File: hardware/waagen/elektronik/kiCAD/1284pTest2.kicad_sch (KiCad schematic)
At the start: 3 parts, among them J3 Conn_02x05_Odd_Even, U6 DS18B20

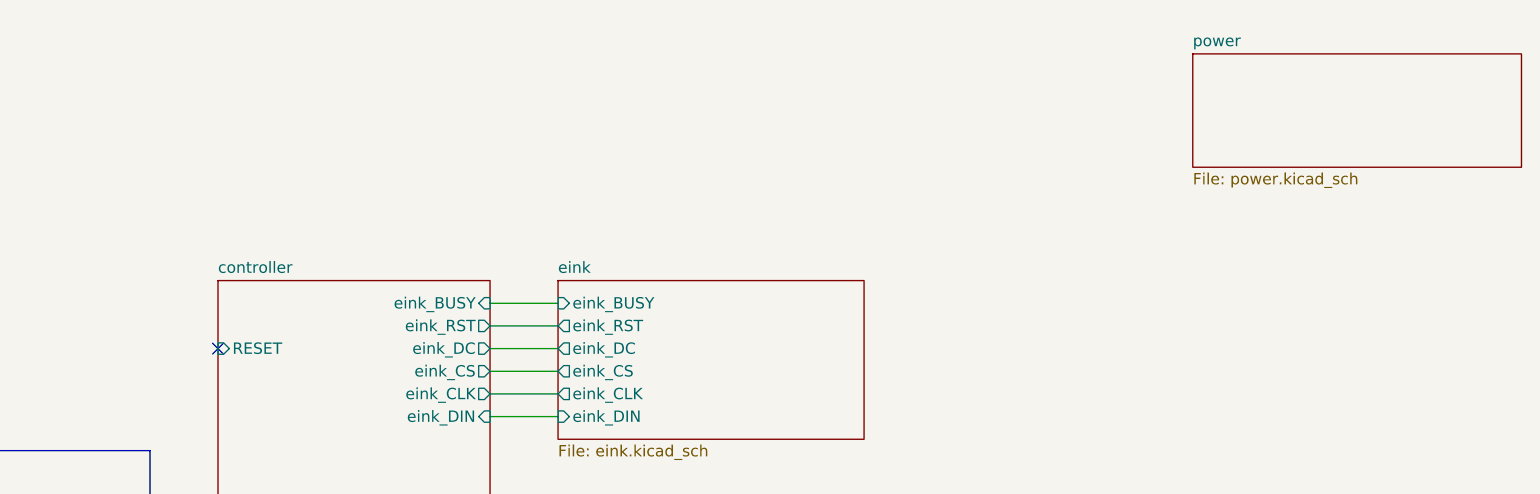
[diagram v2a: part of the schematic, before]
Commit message: second LDO for eink added
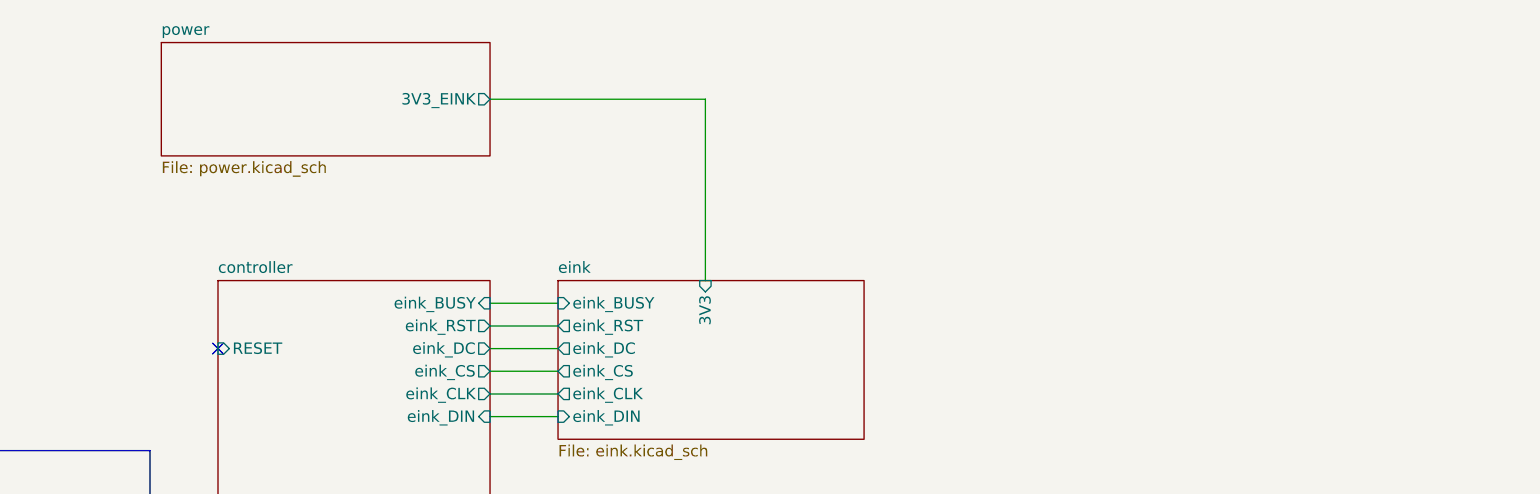
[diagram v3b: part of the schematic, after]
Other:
- sheet eink ports: added 3V3; removed none
- sheet power ports: added 3V3_EINK; removed none
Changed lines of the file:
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@@
+    (stroke (width 0) (type default) (color 0 0 0 0))
+  )
+  (wire (pts (xy 149.86 43.18) (xy 149.86 63.5))
     (stroke (width 0) (type default) (color 0 0 0 0))
   )
@@
   )
   (wire (pts (xy 62.23 93.98) (xy 62.23 95.25))
+    (stroke (width 0) (type default) (color 0 0 0 0))
+  )
+  (wire (pts (xy 125.73 43.18) (xy 149.86 43.18))
     (stroke (width 0) (type default) (color 0 0 0 0))
   )
@@
       (effects (font (size 1.27 1.27)) (justify left))
     )
+    (pin "3V3" input (at 149.86 63.5 90)
+      (effects (font (size 1.27 1.27)) (justify right))
+    )
   )
   (sheet (at 133.35 109.22) (size 34.29 21.59) (fields_autoplaced)
@@
     )
   )
-  (sheet (at 204.47 38.1) (size 36.83 12.7) (fields_autoplaced)
+  (sheet (at 88.9 36.83) (size 36.83 12.7) (fields_autoplaced)
     (stroke (width 0.1524) (type solid) (color 0 0 0 0))
     (fill (color 0 0 0 0.0000))
-    (property "Sheet name" "power" (id 0) (at 204.47 37.3884 0)
+    (property "Sheet name" "power" (id 0) (at 88.9 36.1184 0)
       (effects (font (size 1.27 1.27)) (justify left bottom))
     )
-    (property "Sheet file" "power.kicad_sch" (id 1) (at 204.47 51.3846 0)
+    (property "Sheet file" "power.kicad_sch" (id 1) (at 88.9 50.1146 0)
       (effects (font (size 1.27 1.27)) (justify left top))
+    )
+    (pin "3V3_EINK" output (at 125.73 43.18 0)
+      (effects (font (size 1.27 1.27)) (justify right))
     )
   )
@@
       (reference "#PWR040") (unit 1) (value "GND") (footprint "")
     )
-    (path "/30494837-48ad-4be2-9240-423a5e323ded/63635667-90c7-4555-8fb7-34d9681a99c7"
-      (reference "#PWR041") (unit 1) (value "VCC") (footprint "")
+    (path "/ac84ca8c-8952-41f4-b081-d474e4c76964/6be68c0c-8fc3-4b67-bece-9f51ba607cb0"
+      (reference "#PWR041") (unit 1) (value "GND") (footprint "")
+    )
+    (path "/ac84ca8c-8952-41f4-b081-d474e4c76964/663da0bb-040e-43a6-982a-c4e18537fdce"
+      (reference "#PWR042") (unit 1) (value "GND") (footprint "")
+    )
+    (path "/ac84ca8c-8952-41f4-b081-d474e4c76964/06bfdbdf-3e53-42a3-abc9-fd9ec56e91ec"
+      (reference "#PWR043") (unit 1) (value "GND") (footprint "")
+    )
+    (path "/ac84ca8c-8952-41f4-b081-d474e4c76964/d69a5db1-1044-402e-a9d0-ac8cc7d19c6c"
+      (reference "#PWR044") (unit 1) (value "GND") (footprint "")
+    )
+    (path "/ac84ca8c-8952-41f4-b081-d474e4c76964/1f362bf5-d35e-41ae-9345-c3c2ec77a158"
+      (reference "#PWR045") (unit 1) (value "GND") (footprint "")
+    )
+    (path "/ac84ca8c-8952-41f4-b081-d474e4c76964/5a128969-5504-4d99-8d57-dd94457ee4b6"
+      (reference "#PWR046") (unit 1) (value "GND") (footprint "")
     )
     (path "/43e2f932-9d0d-4a97-af5d-749f39ab369e"
@@
       (reference "C16") (unit 1) (value "100n") (footprint "Capacitor_SMD:C_1206_3216Metric_Pad1.33x1.80mm_HandSolder")
     )
+    (path "/ac84ca8c-8952-41f4-b081-d474e4c76964/ee527360-ce84-4d6c-8892-355abc9d5dd8"
+      (reference "C17") (unit 1) (value "100n") (footprint "Capacitor_SMD:C_1206_3216Metric_Pad1.33x1.80mm_HandSolder")
+    )
+    (path "/ac84ca8c-8952-41f4-b081-d474e4c76964/0fbeb6e5-0120-4f84-8c92-372d91f0d4e4"
+      (reference "C18") (unit 1) (value "10µ") (footprint "Capacitor_SMD:C_1206_3216Metric_Pad1.33x1.80mm_HandSolder")
+    )
+    (path "/ac84ca8c-8952-41f4-b081-d474e4c76964/bca9f2a4-a3e3-4880-b5ae-3091b48b53e1"
+      (reference "C19") (unit 1) (value "1µ") (footprint "Capacitor_SMD:C_1206_3216Metric_Pad1.33x1.80mm_HandSolder")
+    )
+    (path "/ac84ca8c-8952-41f4-b081-d474e4c76964/c7cb3977-8e92-4bf3-b00f-f487f544b100"
+      (reference "C20") (unit 1) (value "1µ") (footprint "Capacitor_SMD:C_1206_3216Metric_Pad1.33x1.80mm_HandSolder")
+    )
     (path "/ac84ca8c-8952-41f4-b081-d474e4c76964/ea7eb0b1-d6f8-4b97-bead-437789c63dd3"
       (reference "D1") (unit 1) (value "LED") (footprint "LED_SMD:LED_1206_3216Metric_Pad1.42x1.75mm_HandSolder")
@@
       (reference "D2") (unit 1) (value "LED") (footprint "LED_SMD:LED_1206_3216Metric_Pad1.42x1.75mm_HandSolder")
     )
+    (path "/ac84ca8c-8952-41f4-b081-d474e4c76964/a3edf98d-14e9-436a-98c4-192509cefb43"
+      (reference "D3") (unit 1) (value "LED") (footprint "LED_SMD:LED_1206_3216Metric_Pad1.42x1.75mm_HandSolder")
+    )
     (path "/ac84ca8c-8952-41f4-b081-d474e4c76964/7c2084e9-3b2e-4e85-bb04-4d1893a867c2"
       (reference "F1") (unit 1) (value "Fuse/Polyfuse 500mA") (footprint "Fuse:Fuse_2512_6332Metric_Pad1.52x3.35mm_HandSolder")
@@
       (reference "R10") (unit 1) (value "4.7k") (footprint "Resistor_SMD:R_1206_3216Metric_Pad1.30x1.75mm_HandSolder")
     )
+    (path "/ac84ca8c-8952-41f4-b081-d474e4c76964/74ba317a-85ad-440e-b769-867e2ba05900"
+      (reference "R11") (unit 1) (value "120") (footprint "Resistor_SMD:R_1206_3216Metric_Pad1.30x1.75mm_HandSolder")
+    )
     (path "/976cd6d7-273a-47c2-827b-7e55ce9fc62e/3da4b1f6-3bca-4457-813a-76de61f61bda"
       (reference "U1") (unit 1) (value "ATmega1284P-P") (footprint "Package_DIP:DIP-40_W15.24mm")
@@
       (reference "U6") (unit 1) (value "DS18B20") (footprint "Package_TO_SOT_THT:TO-92")
     )
+    (path "/ac84ca8c-8952-41f4-b081-d474e4c76964/a5751a47-34cd-4d04-8a2c-6bf019b15822"
+      (reference "U7") (unit 1) (value "MCP1700-3302E_TO92") (footprint "Package_TO_SOT_THT:TO-92_Inline")
+    )
     (path "/976cd6d7-273a-47c2-827b-7e55ce9fc62e/2e767623-5ac9-4a3c-a1df-636aa6d9df7c"

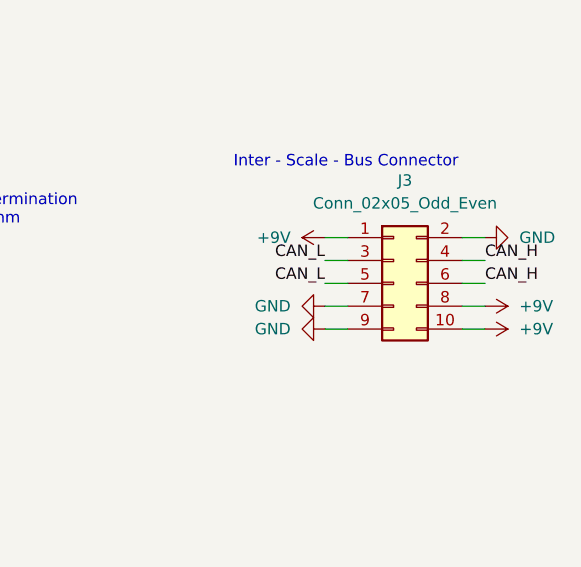
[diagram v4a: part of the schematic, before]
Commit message: Error on JP1 fixed and changed scale wires pads
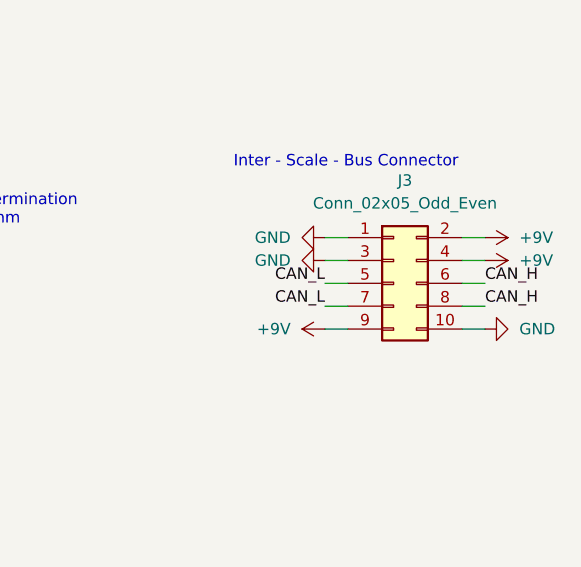
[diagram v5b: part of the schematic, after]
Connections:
- net +9V: now also J3.2 (Pin_2), J3.4 (Pin_4), J3.9 (Pin_9); no longer J3.1 (Pin_1), J3.10 (Pin_10), J3.8 (Pin_8)
- net CAN_H: now also J3.8 (Pin_8); no longer J3.4 (Pin_4)
- net CAN_L: now also J3.7 (Pin_7); no longer J3.3 (Pin_3)
- net GND: now also J3.1 (Pin_1), J3.10 (Pin_10), J3.3 (Pin_3); no longer J3.2 (Pin_2), J3.7 (Pin_7), J3.9 (Pin_9)
